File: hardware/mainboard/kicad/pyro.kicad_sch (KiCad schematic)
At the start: 20 parts, among them J10 J_PYRO2, J4 J_ARM, J9 J_PYRO1, Q3 AO3400A, Q4 AO3400A

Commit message: Platine rev B geroutet: alle 134 Footprints platziert, DRC ohne Fehler, 3 offene Verbindungen; Renders und Lagenbilder; Fertigervergleich
- Lagen: In1 GND, B.Cu geteilte Versorgungsflaeche GND_PWR/5V_SYS, Plane-Vias an jedem SMD-Pad
- Freerouting 2.5.0 (JAR, Temurin 25) mit zwei Nachlaeufen auf fixierter Verdrahtung und kollisionsgeprueften Stummeln
- check_design.py: Netzliste gegen Spezifikation §4 (OK), make.sh fuer die ganze Kette
- 3D-Modelle Teensy 4.1 und XT30PW-M (CadQuery), Renders und layers.pdf in kicad/img
- Fertiger_2026-10-21.md: JLCPCB empfohlen, Aisler als EU-Rueckfall, BMP390 bei JLC nicht lieferbar
- naechster Schritt laut kicad/README.md §8: Review-Punkte A1-A5 (review_kicad_2026-10-21.md) vor dem Handrouting

Co-Authored-By: Claude Opus 5.5 <noreply@anthropic.com>
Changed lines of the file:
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@@
 		(company "Mission Space")
 		(comment 1 "Zwei Pyro-Kanaele low-side, Arming, Durchgangspruefung")
-		(comment 2 "erzeugt von hardware/mainboard/kicad/gen_schematic.py aus circuit.py - nicht von Hand aendern")
+		(comment 2 "erzeugt aus circuit.py (gen_schematic.py)")
 	)
 	(text "Zwei Pyro-Kanaele low-side, Arming, Durchgangspruefung"
@@
 		(stroke (width 0) (type default))
 	)
-	(label "VBAT_ARMED"
+	(global_label "VBAT_ARMED"
+		(shape passive)
 		(at 39.37 46.99 180)
 		(fields_autoplaced yes)
-		(effects (font (size 1.27 1.27)) (justify right bottom))
+		(effects (font (size 1.27 1.27)) (justify right))
 	)
 	(symbol
@@
 		(stroke (width 0) (type default))
 	)
-	(label "VBAT_ARMED"
+	(global_label "VBAT_ARMED"
+		(shape passive)
 		(at 53.34 53.34 90)
 		(fields_autoplaced yes)
-		(effects (font (size 1.27 1.27)) (justify left bottom))
+		(effects (font (size 1.27 1.27)) (justify left))
 	)
 	(wire
@@
 		(stroke (width 0) (type default))
 	)
-	(label "VBAT_ARMED"
+	(global_label "VBAT_ARMED"
+		(shape passive)
 		(at 121.92 44.45 180)
 		(fields_autoplaced yes)
-		(effects (font (size 1.27 1.27)) (justify right bottom))
+		(effects (font (size 1.27 1.27)) (justify right))
 	)
 	(wire
@@
 		(stroke (width 0) (type default))
 	)
-	(label "PYRO1_NEG"
+	(global_label "PYRO1_NEG"
+		(shape passive)
 		(at 121.92 46.99 180)
 		(fields_autoplaced yes)
-		(effects (font (size 1.27 1.27)) (justify right bottom))
+		(effects (font (size 1.27 1.27)) (justify right))
 	)
 	(symbol
@@
 		(stroke (width 0) (type default))
 	)
-	(label "PYRO1_G"
+	(global_label "PYRO1_G"
+		(shape passive)
 		(at 146.05 63.5 180)
 		(fields_autoplaced yes)
-		(effects (font (size 1.27 1.27)) (justify right bottom))
+		(effects (font (size 1.27 1.27)) (justify right))
 	)
 	(wire
@@
 		(stroke (width 0) (type default))
 	)
-	(label "PYRO1_NEG"
+	(global_label "PYRO1_NEG"
+		(shape passive)
 		(at 156.21 55.88 90)
 		(fields_autoplaced yes)
-		(effects (font (size 1.27 1.27)) (justify left bottom))
+		(effects (font (size 1.27 1.27)) (justify left))
 	)
 	(symbol
@@
 		(stroke (width 0) (type default))
 	)
-	(label "PYRO1_G"
+	(global_label "PYRO1_G"
+		(shape passive)
 		(at 162.56 66.04 270)
 		(fields_autoplaced yes)
-		(effects (font (size 1.27 1.27)) (justify right bottom))
+		(effects (font (size 1.27 1.27)) (justify right))
 	)
 	(symbol
@@
 		(stroke (width 0) (type default))
 	)
-	(label "PYRO1_G"
+	(global_label "PYRO1_G"
+		(shape passive)
 		(at 176.53 49.53 90)
 		(fields_autoplaced yes)
-		(effects (font (size 1.27 1.27)) (justify left bottom))
+		(effects (font (size 1.27 1.27)) (justify left))
 	)
 	(wire
@@
 		(stroke (width 0) (type default))
 	)
-	(label "VBAT_ARMED"
+	(global_label "VBAT_ARMED"
+		(shape passive)
 		(at 204.47 44.45 180)
 		(fields_autoplaced yes)
-		(effects (font (size 1.27 1.27)) (justify right bottom))
+		(effects (font (size 1.27 1.27)) (justify right))
 	)
 	(wire
@@
 		(stroke (width 0) (type default))
 	)
-	(label "PYRO1_NEG"
+	(global_label "PYRO1_NEG"
+		(shape passive)
 		(at 217.17 44.45 0)
 		(fields_autoplaced yes)
-		(effects (font (size 1.27 1.27)) (justify left bottom))
+		(effects (font (size 1.27 1.27)) (justify left))
 	)
 	(symbol
@@
 		(stroke (width 0) (type default))
 	)
-	(label "PYRO1_NEG"
+	(global_label "PYRO1_NEG"
+		(shape passive)
 		(at 234.95 52.07 90)
 		(fields_autoplaced yes)
-		(effects (font (size 1.27 1.27)) (justify left bottom))
+		(effects (font (size 1.27 1.27)) (justify left))
 	)
 	(wire
@@
 		(stroke (width 0) (type default))
 	)
-	(label "VBAT_ARMED"
+	(global_label "VBAT_ARMED"
+		(shape passive)
 		(at 39.37 140.97 180)
 		(fields_autoplaced yes)
-		(effects (font (size 1.27 1.27)) (justify right bottom))
+		(effects (font (size 1.27 1.27)) (justify right))
 	)
 	(wire
@@
 		(stroke (width 0) (type default))
 	)
-	(label "PYRO2_NEG"
+	(global_label "PYRO2_NEG"
+		(shape passive)
 		(at 39.37 143.51 180)
 		(fields_autoplaced yes)
-		(effects (font (size 1.27 1.27)) (justify right bottom))
+		(effects (font (size 1.27 1.27)) (justify right))
 	)
 	(symbol
@@
 		(stroke (width 0) (type default))
 	)
-	(label "PYRO2_G"
+	(global_label "PYRO2_G"
+		(shape passive)
 		(at 62.23 160.02 180)
 		(fields_autoplaced yes)
-		(effects (font (size 1.27 1.27)) (justify right bottom))
+		(effects (font (size 1.27 1.27)) (justify right))
 	)
 	(wire
@@
 		(stroke (width 0) (type default))
 	)
-	(label "PYRO2_NEG"
+	(global_label "PYRO2_NEG"
+		(shape passive)
 		(at 72.39 152.4 90)
 		(fields_autoplaced yes)
-		(effects (font (size 1.27 1.27)) (justify left bottom))
+		(effects (font (size 1.27 1.27)) (justify left))
 	)
 	(symbol
@@
 		(stroke (width 0) (type default))
 	)
-	(label "PYRO2_G"
+	(global_label "PYRO2_G"
+		(shape passive)
 		(at 80.01 162.56 270)
 		(fields_autoplaced yes)
-		(effects (font (size 1.27 1.27)) (justify right bottom))
+		(effects (font (size 1.27 1.27)) (justify right))
 	)
 	(symbol
@@
 		(stroke (width 0) (type default))
 	)
-	(label "PYRO2_G"
+	(global_label "PYRO2_G"
+		(shape passive)
 		(at 93.98 146.05 90)
 		(fields_autoplaced yes)
-		(effects (font (size 1.27 1.27)) (justify left bottom))
+		(effects (font (size 1.27 1.27)) (justify left))
 	)
 	(wire
@@
 		(stroke (width 0) (type default))
 	)
-	(label "VBAT_ARMED"
+	(global_label "VBAT_ARMED"
+		(shape passive)
 		(at 121.92 140.97 180)
 		(fields_autoplaced yes)
-		(effects (font (size 1.27 1.27)) (justify right bottom))
+		(effects (font (size 1.27 1.27)) (justify right))
 	)
 	(wire
@@
 		(stroke (width 0) (type default))
 	)
-	(label "PYRO2_NEG"
+	(global_label "PYRO2_NEG"
+		(shape passive)
 		(at 134.62 140.97 0)
 		(fields_autoplaced yes)
-		(effects (font (size 1.27 1.27)) (justify left bottom))
+		(effects (font (size 1.27 1.27)) (justify left))
 	)
 	(symbol
@@
 		(stroke (width 0) (type default))
 	)
-	(label "PYRO2_NEG"
+	(global_label "PYRO2_NEG"
+		(shape passive)
 		(at 152.4 148.59 90)
 		(fields_autoplaced yes)
-		(effects (font (size 1.27 1.27)) (justify left bottom))
-	)
-	(wire
+		(effects (font (size 1.27 1.27)) (justify left))
+	)
+	(wire

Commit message: Kartonaut: Name, Missionsabzeichen, Bestückungsdruck neu, Lötstopp blau
- Projekt heißt Kartonaut (Karton + Astronaut); Flüge werden hochgezählt, Erstflug = Kartonaut 1
- Abzeichen als Polygone in hardware/mainboard/kicad/logo.py, SVGs in docs/brand/
- spacecode/ -> firmware/, Bodenstation-Repo groundcode -> kartonaut-ground (Links, .gitignore)
- gen_pcb.py silk: Bestückungsdruck nur neu setzen, auf der gerouteten Platine; 1,0 mm Schrift,
  freie Plätze statt Überlappungen, Kurznamen an den Steckern, Testpunkte mit Netznamen,
  kleines Abzeichen vorn; hinten Abzeichen 20 mm und Steckerbelegung
- Stackup JLC04161H-7628 mit blauem Lötstopp im Board, Renders mit Stackup-Farben
- DRC-Druckwarnungen 167 -> 14 (Rest aus Footprint-Umrissen)

Co-Authored-By: Claude Opus 5.5 <noreply@anthropic.com>
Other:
- company: Mission Space -> Kartonaut
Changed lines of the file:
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@@
 		(date "2026-10-21")
 		(rev "B")
-		(company "Mission Space")
+		(company "Kartonaut")
 		(comment 1 "Zwei Pyro-Kanaele low-side, Arming, Durchgangspruefung")
 		(comment 2 "erzeugt aus circuit.py (gen_schematic.py)")

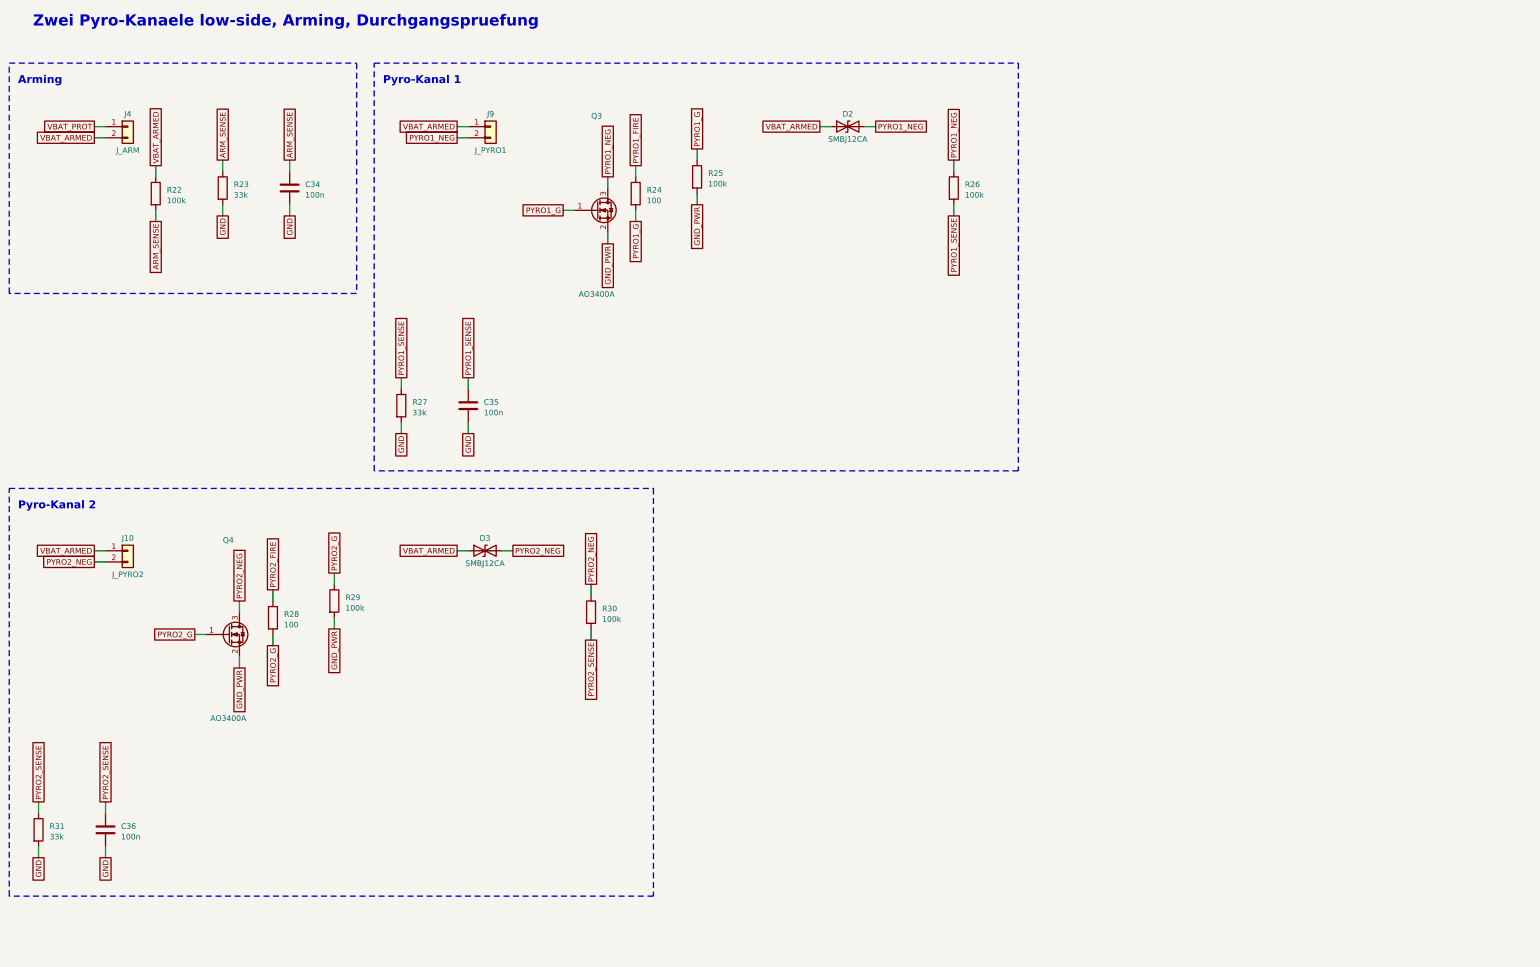
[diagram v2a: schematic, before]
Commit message: Mainboard rev B1: Review A1-A8 und Entscheidungen E1-E10 eingearbeitet, 2S-Pfad als F.Cu-Flaechen, 28 Verbindungen offen
Schaltung (circuit.py, ERC 0, Netzliste gegen README §4 OK): Hold-up hinter D1, EN-Teiler 330k/115k,
P-FET-Lastschalter je Akku, Polyfuse je Akku, Kelvin-Shunt mit INA239 an SPI1, BMP390 an SPI1,
74HC138/74HC4051 mit gemeinsamer Adresse, J_STACK 2x10 mit LDO 3V3_EXP, 1S-Lader MCP73831,
J_CHG2, vier Pyro-Kanaele (3/4 DNP), vierter Servo, alle Servos und Rollmotor an VSERVO,
3V3_SENS, eine WS2812B-Kette, Summer Pin 37, E22 NRST Pin 6; 166 Bauteile.

Platine (gen_pcb.py): neue Platzierung, 2S-Pfad, Pyro-Ausgaenge und VSYS_IN als F.Cu-Flaechen mit
Sperrflaechen fuer Freerouting, Strom-Klasse nur F.Cu, IMU-Zone 5 mm, patch mit Umweg ueber In2.
DRC 0 Fehler, Paritaet 0, kein 2S-Netz auf In2; 28 offene Verbindungen, Liste in kicad/README.md §5.5.
Spezifikation README.md und kicad/README.md auf B1 nachgezogen, review_check_layout.py fuer B1.

Co-Authored-By: Claude Opus 5.5 <noreply@anthropic.com>
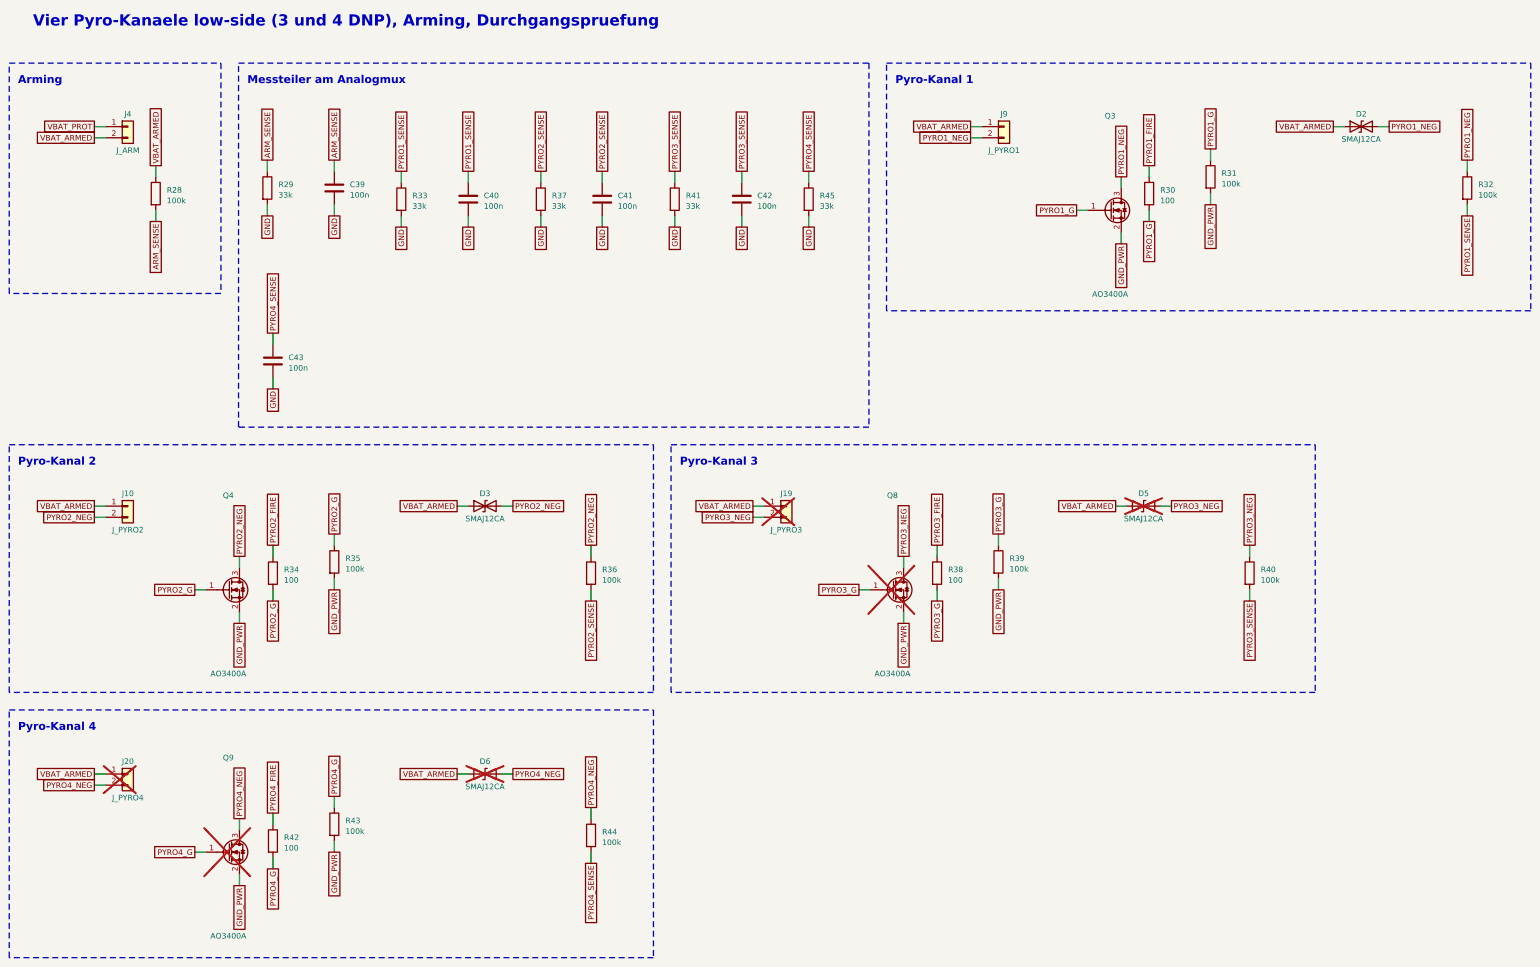
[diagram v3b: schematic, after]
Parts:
- removed C34, C35, C36: 100n, Capacitor_SMD:C_0603_1608Metric, symbol Device:C
- removed R22, R25, R26: 100k, Resistor_SMD:R_0603_1608Metric, symbol Device:R
- removed R23, R27: 33k, Resistor_SMD:R_0603_1608Metric, symbol Device:R
- removed R24: 100, Resistor_SMD:R_0603_1608Metric, symbol Device:R
- added C39, C40, C41, C42, C43: 100n, Capacitor_SMD:C_0603_1608Metric, symbol Device:C
- added D5, D6: SMAJ12CA, Diode_SMD:D_SMA, symbol Device:D_TVS
- added J19: J_PYRO3, Connector_JST:JST_XH_S2B-XH-A_1x02_P2.50mm_Horizontal, symbol Connector_Generic:Conn_01x02
- added J20: J_PYRO4, Connector_JST:JST_XH_S2B-XH-A_1x02_P2.50mm_Horizontal, symbol Connector_Generic:Conn_01x02
- added Q8, Q9: AO3400A, Package_TO_SOT_SMD:SOT-23, symbol Transistor_FET:AO3400A
- added R32, R35, R36, R39, R40, R43, R44: 100k, Resistor_SMD:R_0603_1608Metric, symbol Device:R
- added R33, R37, R41, R45: 33k, Resistor_SMD:R_0603_1608Metric, symbol Device:R
- added R34, R38, R42: 100, Resistor_SMD:R_0603_1608Metric, symbol Device:R
- D2, D3: value SMBJ12CA -> SMAJ12CA; footprint Diode_SMD:D_SMB -> Diode_SMD:D_SMA
- J4: footprint Connector_JST:JST_PH_S2B-PH-K_1x02_P2.00mm_Horizontal -> Connector_JST:JST_XH_B2B-XH-A_1x02_P2.50mm_Vertical
- R28: value 100 -> 100k
- R29: value 100k -> 33k
- R30: value 100k -> 100
- R31: value 33k -> 100k
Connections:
- net ARM_SENSE: now also R28.2, R29.1, C39.1
- net GND: now also R29.2, C39.2, C40.2, C41.2, C42.2, C43.2, R33.2, R37.2, R41.2, R45.2; no longer R31.2
- net GND_PWR: now also R31.2, Q8.2 (S), Q9.2 (S), R35.2, R39.2, R43.2; no longer R29.2
- net PYRO1_FIRE: now also R30.1
- net PYRO1_G: now also R30.2, R31.1
- net PYRO1_NEG: now also R32.1
- net PYRO1_SENSE: now also C40.1, R32.2, R33.1
- net PYRO2_FIRE: now also R34.1; no longer R28.1
- net PYRO2_G: now also R34.2, R35.1; no longer R28.2, R29.1
- net PYRO2_NEG: now also R36.1; no longer R30.1
- net PYRO2_SENSE: now also C41.1, R36.2, R37.1; no longer R30.2, R31.1
- net VBAT_ARMED: now also R28.1, D5.1 (A1), D6.1 (A1), J19.1 (Pin_1), J20.1 (Pin_1)
- new net PYRO3_FIRE: R38.1
- new net PYRO3_G: Q8.1 (G), R38.2, R39.1
- new net PYRO3_NEG: D5.2 (A2), J19.2 (Pin_2), Q8.3 (D), R40.1
- new net PYRO3_SENSE: C42.1, R40.2, R41.1
- new net PYRO4_FIRE: R42.1
- new net PYRO4_G: Q9.1 (G), R42.2, R43.1
- new net PYRO4_NEG: D6.2 (A2), J20.2 (Pin_2), Q9.3 (D), R44.1
- new net PYRO4_SENSE: C43.1, R44.2, R45.1
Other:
- note added: "Messteiler am Analogmux"
- note added: "Pyro-Kanal 3"
- note added: "Pyro-Kanal 4"
- note added: "Vier Pyro-Kanaele low-side (3 und 4 DNP), Arming, Durchgangspruefung"
- note removed: "Zwei Pyro-Kanaele low-side, Arming, Durchgangspruefung"
- moved on the sheet: D2, D3, J10, J9, Q3, Q4, R28, R29, R30, R31
